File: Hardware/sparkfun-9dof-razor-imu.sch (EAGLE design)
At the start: 54 parts, among them J1 LiPo, J3 USD_CONNECTOR, U1 3.3V, U2 MCP73831, U3 MPU-9250", U4 ATSAMD21G-A, Y1 32.768kHz

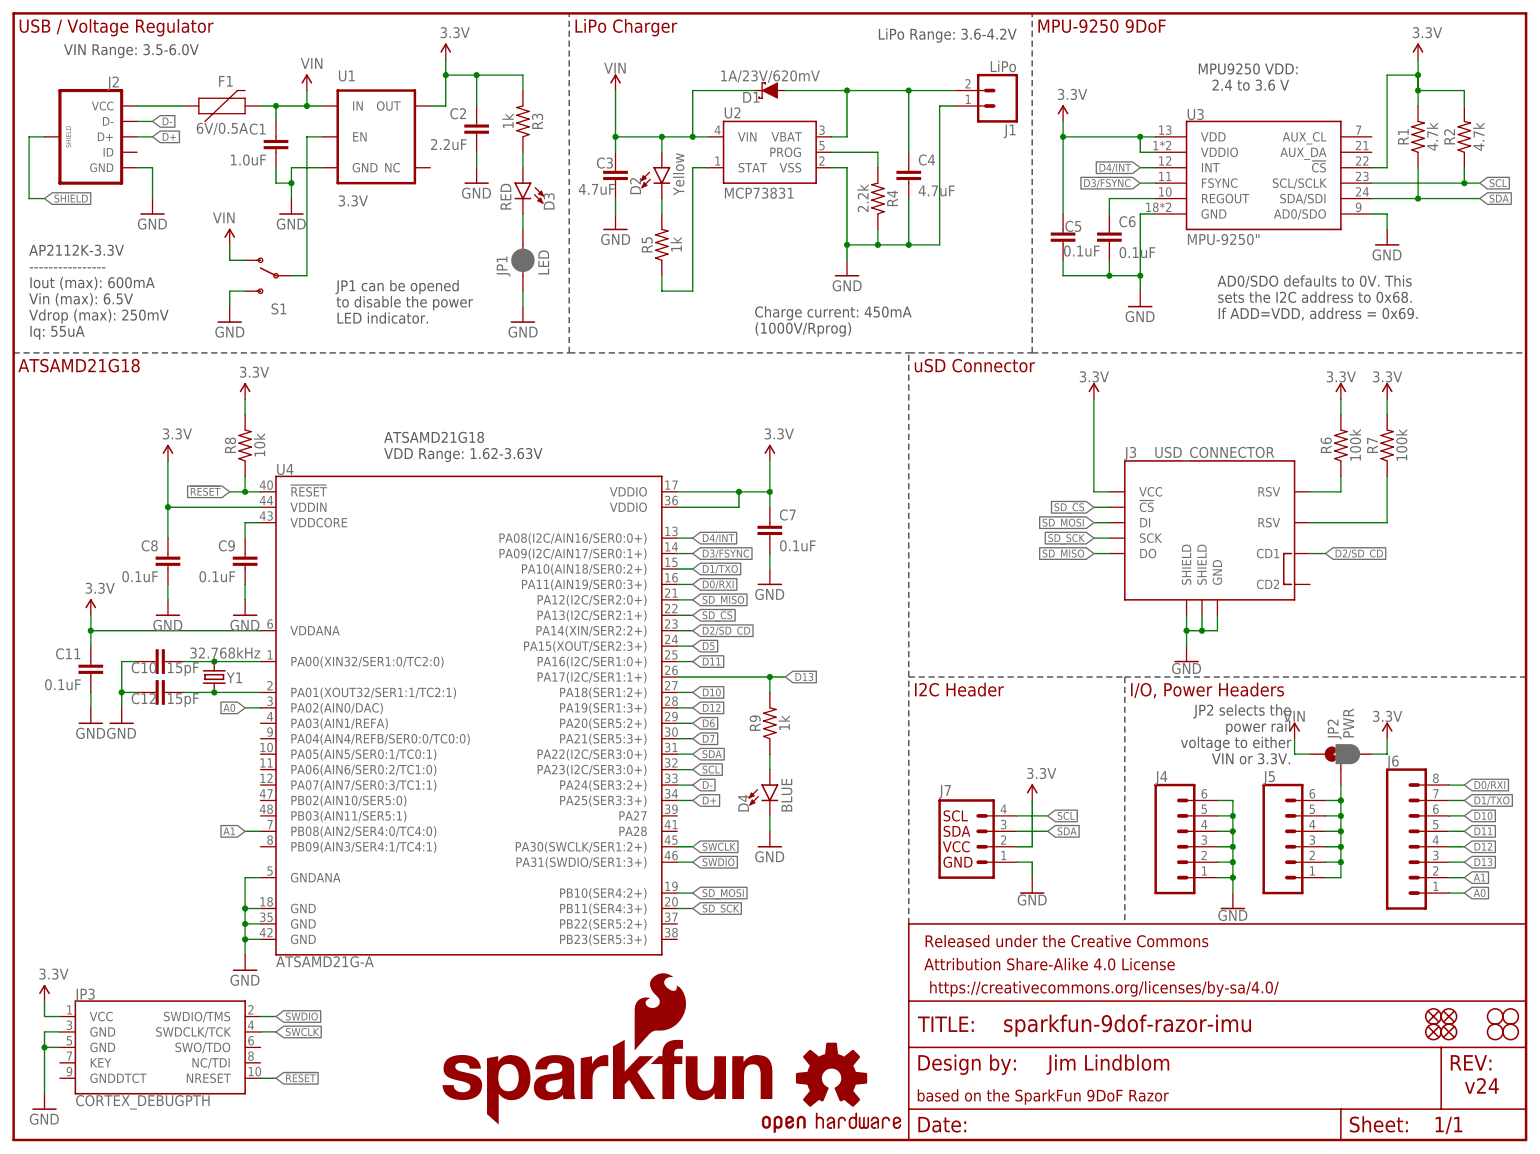
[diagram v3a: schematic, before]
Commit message: Reorganizing expansion header(s), layout cleanup, PROD_ID's.
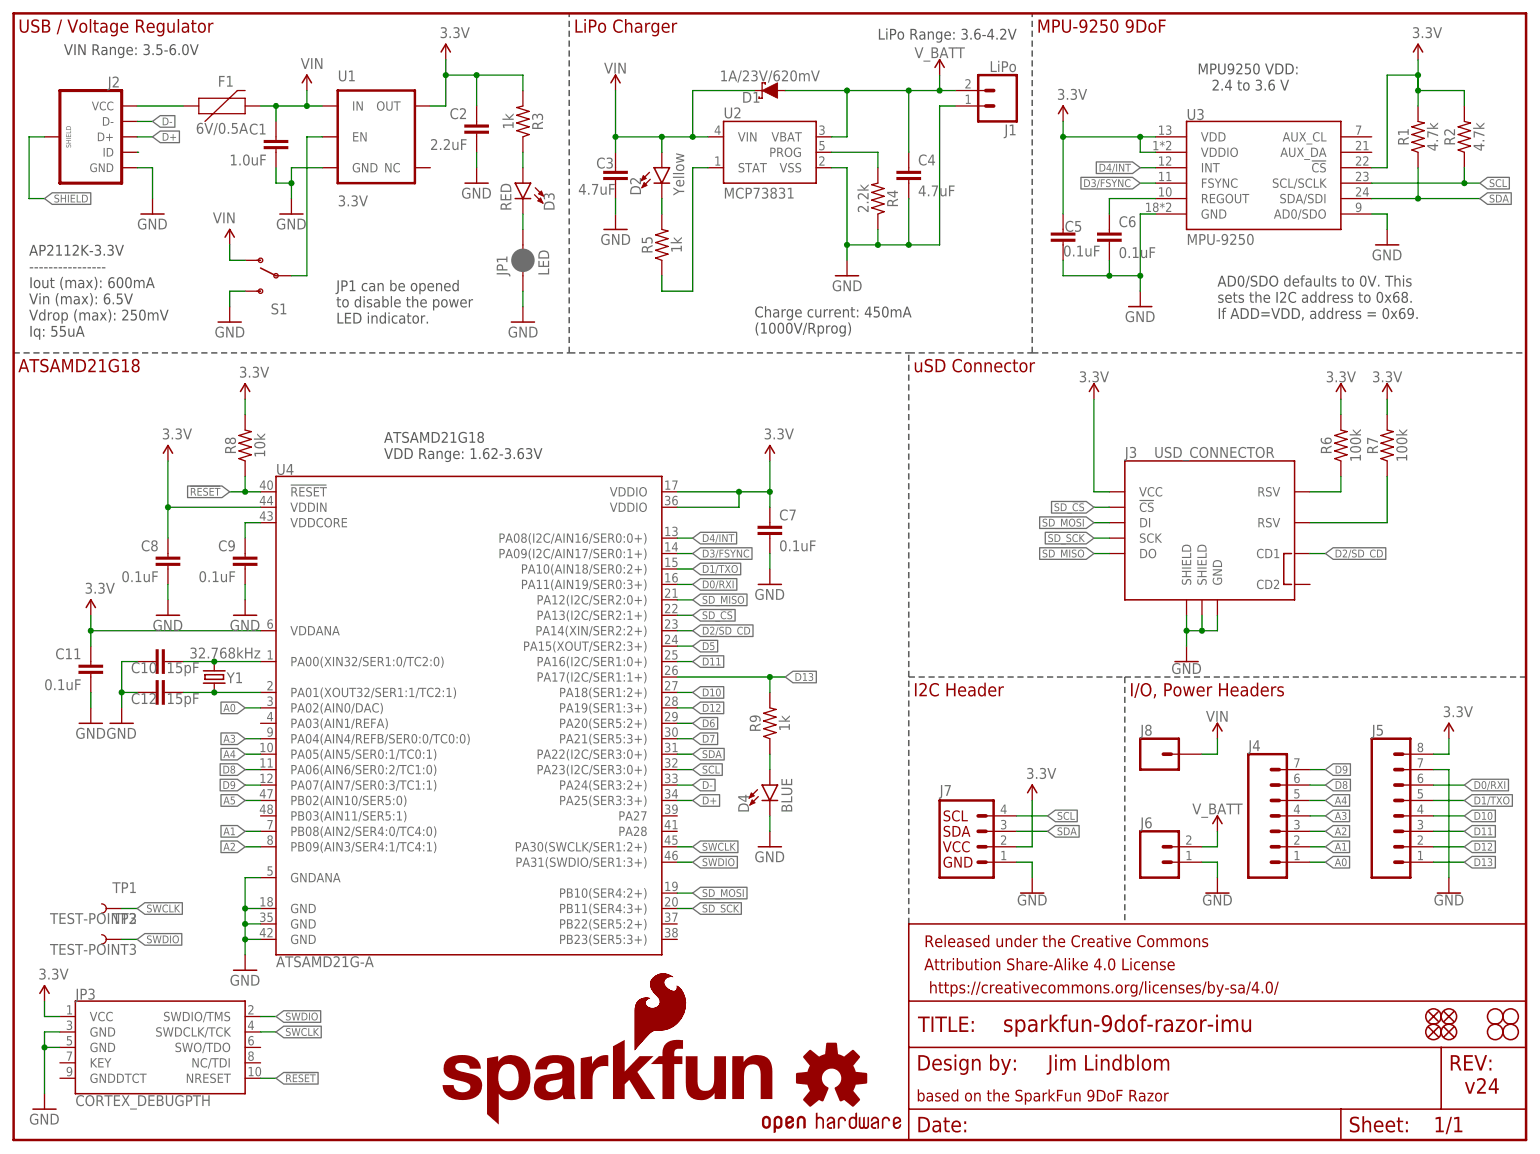
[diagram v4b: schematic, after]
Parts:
- removed JP2: PWR, SparkFun-Jumpers:JUMPER-SMT_3_1-NC_PASTE_NO-SILK
- added J8: (no value), SparkFun-Connectors:CONN_01
- added LOGO4: SFE_LOGO_FLAME.1_INCH, SparkFun-Aesthetics:SFE_LOGO_FLAME.1_INCH
- added TP1, TP2: TEST-POINT3, SparkFun-Connectors:TEST-POINT3
- J4: device SparkFun-Connectors:CONN_06NO_SILK_FEMALE_PTH -> SparkFun-Connectors:CONN_07
- J5: device SparkFun-Connectors:CONN_06NO_SILK_FEMALE_PTH -> SparkFun-Connectors:CONN_08"
- J6: device SparkFun-Connectors:CONN_08" -> SparkFun-Connectors:CONN_02
- U3: value MPU-9250" -> MPU-9250; device 9dof-devboard-temp:MPU-9250" -> 9dof-devboard-temp:MPU-9250
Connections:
- removed net N$10: C4.1, D1.A, J1.1, U2.VBAT
- removed net N$6: J5.1, J5.2, J5.3, J5.4, J5.5, J5.6, JP2.2
- new net A2: J4.3, U4.PB09(AIN3/SER4:1/TC4:1)
- new net A3: J4.4, U4.PA04(AIN4/REFB/SER0:0/TC0:0)
- new net A4: J4.5, U4.PA05(AIN5/SER0:1/TC0:1)
- new net A5: U4.PB02(AIN10/SER5:0)
- new net D8: J4.6, U4.PA06(AIN6/SER0:2/TC1:0)
- new net D9: J4.7, U4.PA07(AIN7/SER0:3/TC1:1)
- new net ID: J2.ID
- new net V_BATT: C4.1, D1.A, J1.1, J6.2, U2.VBAT
- net 3.3V: now also J5.8; no longer JP2.3
- net A0: now also J4.1; no longer J6.1
- net A1: now also J4.2; no longer J6.2
- net D0/RXI: now also J5.6; no longer J6.8
- net D1/TXO: now also J5.5; no longer J6.7
- net D10: now also J5.4; no longer J6.6
- net D11: now also J5.3; no longer J6.5
- net D12: now also J5.2; no longer J6.4
- net D13: now also J5.1; no longer J6.3
- net GND: now also J5.7, J6.1; no longer J4.1, J4.2, J4.3, J4.4, J4.5, J4.6
- net SWCLK: now also TP1.1
- net SWDIO: now also TP2.1
- net VIN: now also J8.1; no longer JP2.1
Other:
- note removed: "JP2 selects the power rail voltage to either VIN or 3.3V."

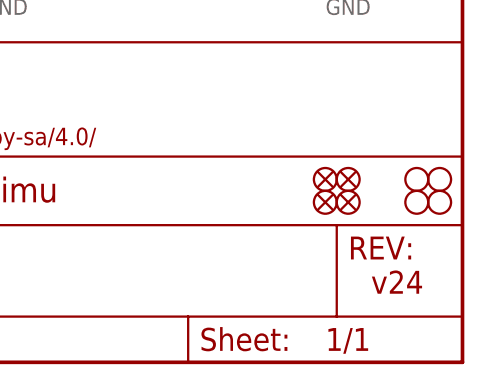
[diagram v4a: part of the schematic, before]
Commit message: Updating version number to redboard release - v30
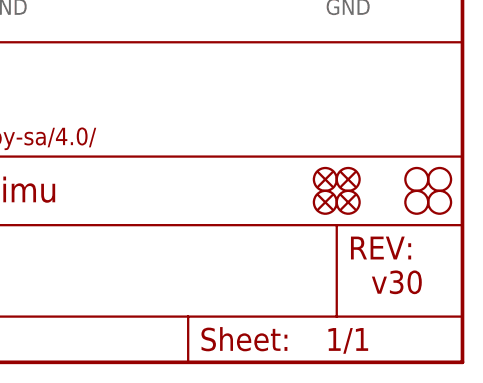
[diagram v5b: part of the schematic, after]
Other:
- note added: "v30"
- note removed: "v24"
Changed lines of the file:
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@@
 <grid distance="0.1" unitdist="inch" unit="inch" style="lines" multiple="1" display="no" altdistance="0.01" altunitdist="inch" altunit="inch"/>
 <layers>
-<layer number="1" name="Top" color="4" fill="1" visible="yes" active="no"/>
-<layer number="2" name="Route2" color="1" fill="3" visible="yes" active="no"/>
-<layer number="3" name="Route3" color="4" fill="3" visible="yes" active="no"/>
-<layer number="4" name="Route4" color="1" fill="4" visible="yes" active="no"/>
-<layer number="5" name="Route5" color="4" fill="4" visible="yes" active="no"/>
-<layer number="6" name="Route6" color="1" fill="8" visible="yes" active="no"/>
-<layer number="7" name="Route7" color="4" fill="8" visible="yes" active="no"/>
-<layer number="8" name="Route8" color="1" fill="2" visible="yes" active="no"/>
-<layer number="9" name="Route9" color="4" fill="2" visible="yes" active="no"/>
-<layer number="10" name="Route10" color="1" fill="7" visible="yes" active="no"/>
-<layer number="11" name="Route11" color="4" fill="7" visible="yes" active="no"/>
-<layer number="12" name="Route12" color="1" fill="5" visible="yes" active="no"/>
-<layer number="13" name="Route13" color="4" fill="5" visible="yes" active="no"/>
-<layer number="14" name="Route14" color="1" fill="6" visible="yes" active="no"/>
-<layer number="15" name="Route15" color="4" fill="6" visible="yes" active="no"/>
-<layer number="16" name="Bottom" color="1" fill="1" visible="yes" active="no"/>
-<layer number="17" name="Pads" color="2" fill="1" visible="yes" active="no"/>
-<layer number="18" name="Vias" color="2" fill="1" visible="yes" active="no"/>
-<layer number="19" name="Unrouted" color="6" fill="1" visible="yes" active="no"/>
-<layer number="20" name="Dimension" color="15" fill="1" visible="yes" active="no"/>
-<layer number="21" name="tPlace" color="16" fill="1" visible="yes" active="no"/>
-<layer number="22" name="bPlace" color="14" fill="1" visible="yes" active="no"/>
-<layer number="23" name="tOrigins" color="15" fill="1" visible="yes" active="no"/>
-<layer number="24" name="bOrigins" color="15" fill="1" visible="yes" active="no"/>
-<layer number="25" name="tNames" color="7" fill="1" visible="yes" active="no"/>
-<layer number="26" name="bNames" color="7" fill="1" visible="yes" active="no"/>
-<layer number="27" name="tValues" color="7" fill="1" visible="yes" active="no"/>
-<layer number="28" name="bValues" color="7" fill="1" visible="yes" active="no"/>
+<layer number="1" name="Top" color="4" fill="1" visible="no" active="no"/>
+<layer number="2" name="Route2" color="1" fill="3" visible="no" active="no"/>
+<layer number="3" name="Route3" color="4" fill="3" visible="no" active="no"/>
+<layer number="4" name="Route4" color="1" fill="4" visible="no" active="no"/>
+<layer number="5" name="Route5" color="4" fill="4" visible="no" active="no"/>
+<layer number="6" name="Route6" color="1" fill="8" visible="no" active="no"/>
+<layer number="7" name="Route7" color="4" fill="8" visible="no" active="no"/>
+<layer number="8" name="Route8" color="1" fill="2" visible="no" active="no"/>
+<layer number="9" name="Route9" color="4" fill="2" visible="no" active="no"/>
+<layer number="10" name="Route10" color="1" fill="7" visible="no" active="no"/>
+<layer number="11" name="Route11" color="4" fill="7" visible="no" active="no"/>
+<layer number="12" name="Route12" color="1" fill="5" visible="no" active="no"/>
+<layer number="13" name="Route13" color="4" fill="5" visible="no" active="no"/>
+<layer number="14" name="Route14" color="1" fill="6" visible="no" active="no"/>
+<layer number="15" name="Route15" color="4" fill="6" visible="no" active="no"/>
+<layer number="16" name="Bottom" color="1" fill="1" visible="no" active="no"/>
+<layer number="17" name="Pads" color="2" fill="1" visible="no" active="no"/>
+<layer number="18" name="Vias" color="2" fill="1" visible="no" active="no"/>
+<layer number="19" name="Unrouted" color="6" fill="1" visible="no" active="no"/>
+<layer number="20" name="Dimension" color="15" fill="1" visible="no" active="no"/>
+<layer number="21" name="tPlace" color="16" fill="1" visible="no" active="no"/>
+<layer number="22" name="bPlace" color="14" fill="1" visible="no" active="no"/>
+<layer number="23" name="tOrigins" color="15" fill="1" visible="no" active="no"/>
+<layer number="24" name="bOrigins" color="15" fill="1" visible="no" active="no"/>
+<layer number="25" name="tNames" color="7" fill="1" visible="no" active="no"/>
+<layer number="26" name="bNames" color="7" fill="1" visible="no" active="no"/>
+<layer number="27" name="tValues" color="7" fill="1" visible="no" active="no"/>
+<layer number="28" name="bValues" color="7" fill="1" visible="no" active="no"/>
 <layer number="29" name="tStop" color="7" fill="3" visible="no" active="no"/>
 <layer number="30" name="bStop" color="7" fill="6" visible="no" active="no"/>
@@
 <layer number="35" name="tGlue" color="7" fill="4" visible="no" active="no"/>
 <layer number="36" name="bGlue" color="7" fill="5" visible="no" active="no"/>
-<layer number="37" name="tTest" color="7" fill="1" visible="yes" active="no"/>
-<layer number="38" name="bTest" color="7" fill="1" visible="yes" active="no"/>
+<layer number="37" name="tTest" color="7" fill="1" visible="no" active="no"/>
+<layer number="38" name="bTest" color="7" fill="1" visible="no" active="no"/>
 <layer number="39" name="tKeepout" color="4" fill="11" visible="no" active="no"/>
 <layer number="40" name="bKeepout" color="1" fill="11" visible="no" active="no"/>
@@
 <layer number="44" name="Drills" color="7" fill="1" visible="no" active="no"/>
 <layer number="45" name="Holes" color="7" fill="1" visible="no" active="no"/>
-<layer number="46" name="Milling" color="3" fill="1" visible="yes" active="no"/>
-<layer number="47" name="Measures" color="7" fill="1" visible="yes" active="no"/>
-<layer number="48" name="Document" color="7" fill="1" visible="yes" active="no"/>
-<layer number="49" name="Reference" color="7" fill="1" visible="yes" active="no"/>
-<layer number="50" name="dxf" color="7" fill="1" visible="yes" active="no"/>
-<layer number="51" name="tDocu" color="6" fill="1" visible="yes" active="no"/>
-<layer number="52" name="bDocu" color="7" fill="1" visible="yes" active="no"/>
-<layer number="53" name="tGND_GNDA" color="7" fill="9" visible="yes" active="no"/>
-<layer number="54" name="bGND_GNDA" color="1" fill="9" visible="yes" active="no"/>
-<layer number="56" name="wert" color="7" fill="1" visible="yes" active="no"/>
-<layer number="57" name="tCAD" color="7" fill="1" visible="yes" active="no"/>
-<layer number="59" name="tCarbon" color="7" fill="1" visible="yes" active="no"/>
-<layer number="60" name="bCarbon" color="7" fill="1" visible="yes" active="no"/>
+<layer number="46" name="Milling" color="3" fill="1" visible="no" active="no"/>
+<layer number="47" name="Measures" color="7" fill="1" visible="no" active="no"/>
+<layer number="48" name="Document" color="7" fill="1" visible="no" active="no"/>
+<layer number="49" name="Reference" color="7" fill="1" visible="no" active="no"/>
+<layer number="50" name="dxf" color="7" fill="1" visible="no" active="no"/>
+<layer number="51" name="tDocu" color="6" fill="1" visible="no" active="no"/>
+<layer number="52" name="bDocu" color="7" fill="1" visible="no" active="no"/>
+<layer number="53" name="tGND_GNDA" color="7" fill="9" visible="no" active="no"/>
+<layer number="54" name="bGND_GNDA" color="1" fill="9" visible="no" active="no"/>
+<layer number="56" name="wert" color="7" fill="1" visible="no" active="no"/>
+<layer number="57" name="tCAD" color="7" fill="1" visible="no" active="no"/>
+<layer number="59" name="tCarbon" color="7" fill="1" visible="no" active="no"/>
+<layer number="60" name="bCarbon" color="7" fill="1" visible="no" active="no"/>
 <layer number="90" name="Modules" color="5" fill="1" visible="yes" active="yes"/>
 <layer number="91" name="Nets" color="2" fill="1" visible="yes" active="yes"/>
@@
 Vdrop (max): 250mV
 Iq: 55uA</text>
-<text x="238.76" y="7.62" size="2.54" layer="94">v24</text>
+<text x="238.76" y="7.62" size="2.54" layer="94">v30</text>
 <text x="170.18" y="11.43" size="2.54" layer="94">Jim Lindblom</text>
 <wire x1="0" y1="129.54" x2="91.44" y2="129.54" width="0.254" layer="97" style="shortdash"/>

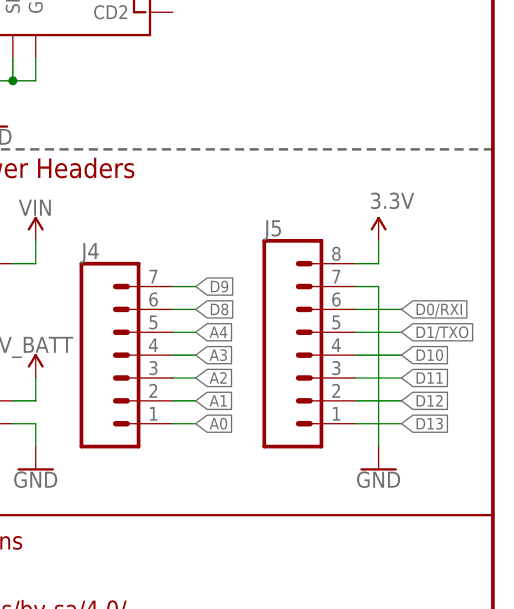
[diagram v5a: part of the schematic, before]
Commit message: Post-review changes - swapping 3.3V and GND, moving switch in.
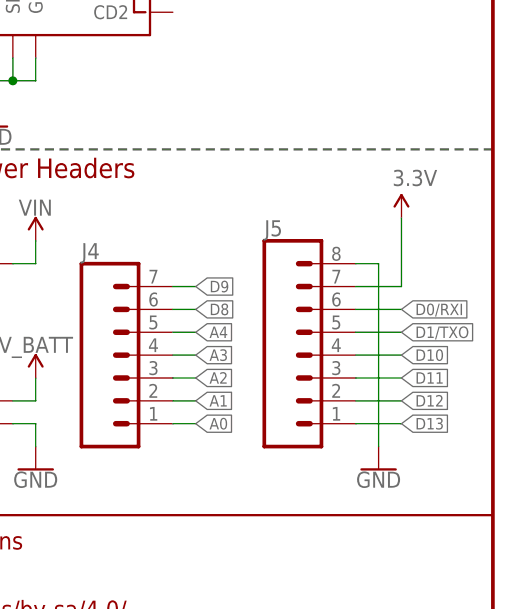
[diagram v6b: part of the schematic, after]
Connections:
- net 3.3V: now also J5.7; no longer J5.8
- net GND: now also J5.8; no longer J5.7
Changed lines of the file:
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@@
 <instance part="SUPPLY14" gate="G$1" x="152.4" y="175.26"/>
 <instance part="J5" gate="G$1" x="228.6" y="53.34"/>
-<instance part="SUPPLY15" gate="G$1" x="236.22" y="66.04"/>
+<instance part="SUPPLY15" gate="G$1" x="238.76" y="68.58"/>
 <instance part="GND18" gate="1" x="236.22" y="40.64"/>
 <instance part="J4" gate="G$1" x="208.28" y="50.8"/>
@@
 </segment>
 <segment>
-<pinref part="J5" gate="G$1" pin="7"/>
-<wire x1="233.68" y1="60.96" x2="236.22" y2="60.96" width="0.1524" layer="91"/>
 <pinref part="GND18" gate="1" pin="GND"/>
-<wire x1="236.22" y1="60.96" x2="236.22" y2="43.18" width="0.1524" layer="91"/>
+<wire x1="236.22" y1="63.5" x2="236.22" y2="43.18" width="0.1524" layer="91"/>
+<pinref part="J5" gate="G$1" pin="8"/>
+<wire x1="236.22" y1="63.5" x2="233.68" y2="63.5" width="0.1524" layer="91"/>
 </segment>
 <segment>
@@
 </segment>
 <segment>
-<pinref part="J5" gate="G$1" pin="8"/>
-<wire x1="233.68" y1="63.5" x2="236.22" y2="63.5" width="0.1524" layer="91"/>
-<wire x1="236.22" y1="63.5" x2="236.22" y2="66.04" width="0.1524" layer="91"/>
 <pinref part="SUPPLY15" gate="G$1" pin="3.3V"/>
+<pinref part="J5" gate="G$1" pin="7"/>
+<wire x1="233.68" y1="60.96" x2="238.76" y2="60.96" width="0.1524" layer="91"/>
+<wire x1="238.76" y1="60.96" x2="238.76" y2="68.58" width="0.1524" layer="91"/>
 </segment>
 </net>
